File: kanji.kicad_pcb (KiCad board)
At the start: 2 copper layers, 105.3 x 70.8 mm, 30 parts, among them J3 E-Ink, Q1 AO3400A, U3 SHT4x, U4 XIAO-ESP32-S3-SMD

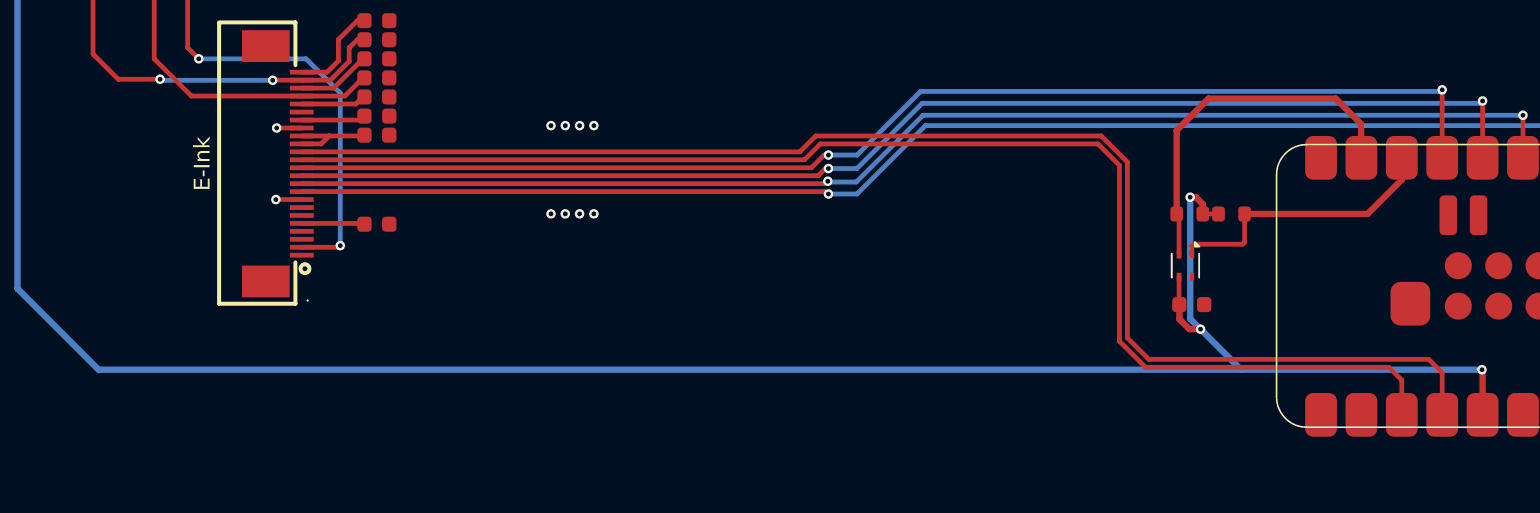
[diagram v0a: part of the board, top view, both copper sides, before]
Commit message: feat: add light sensor
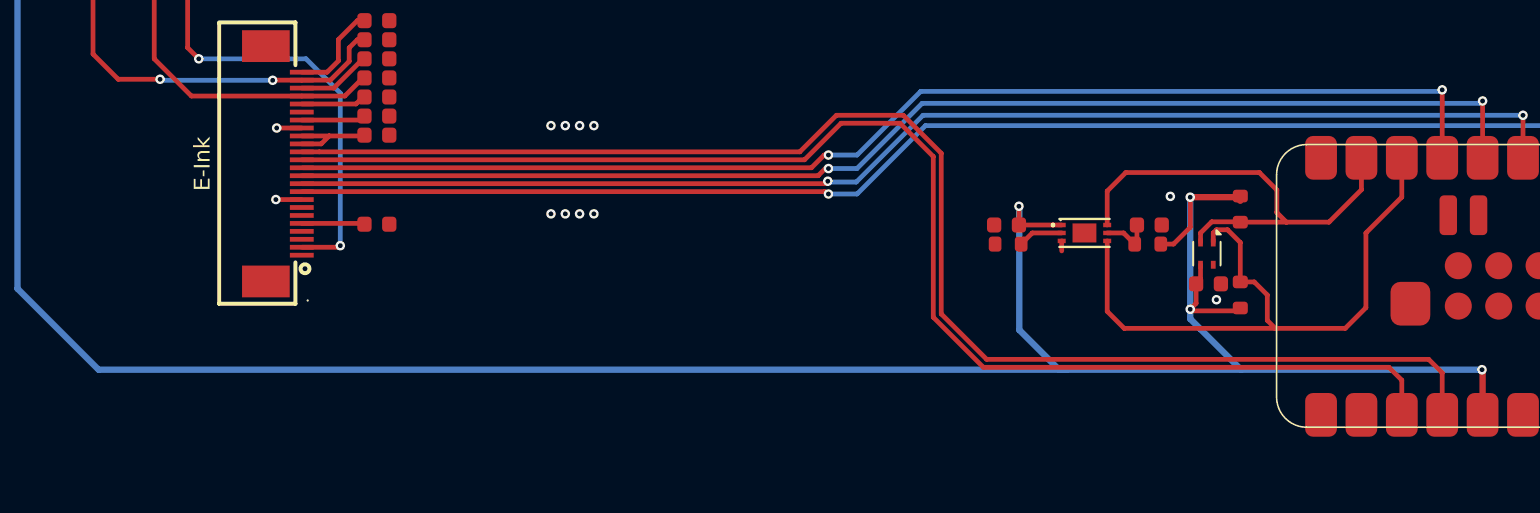
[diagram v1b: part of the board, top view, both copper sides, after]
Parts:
- removed R7, R8: 10kΩ, PCM_JLCPCB:R_0603
- added C1: 100nF, PCM_JLCPCB:C_0603, F.Cu at (175.6, 98.1)
- added C17: 100nF, PCM_JLCPCB:C_0603, F.Cu at (166.6, 98.1)
- added R1: 4.7kΩ, PCM_JLCPCB:R_0603, F.Cu at (166.7, 99.3)
- added R10: 4.7kΩ, PCM_JLCPCB:R_0603, F.Cu at (181.3, 102.5)
- added R2: 1kΩ, PCM_JLCPCB:R_0603, F.Cu at (175.5, 99.3)
- added R9: 4.7kΩ, PCM_JLCPCB:R_0603, F.Cu at (181.3, 97.1)
- added U1: BH1750FVI-TR, easyeda2kicad:WSOF-6_L2.6-W1.6-P0.50-TL-EP, F.Cu at (171.5, 98.6)
- moved C16 1.68 mm to (179.3, 101.8)
- moved U3 1.55 mm to (179.2, 99.9)
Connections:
- net /SHT40-SCL renamed /SCL
- net /SHT40-SDA renamed /SDA
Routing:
- net /SDA: track 17.9 -> 41.6 mm
- net +3V3: track 156.3 -> 178.9 mm, vias 4 -> 5
- net /SCL: track 23.1 -> 29.9 mm
- net Net-(U1-DVI): track 0.00 -> 3.28 mm
- net Net-(U1-ADDR): track 0.00 -> 2.84 mm
- net GND: track 3.21 -> 3.84 mm, vias 10 -> 12
- net /DATA: track 87.4 -> 87.9 mm
- net /CLK: track 84.4 -> 84.9 mm
